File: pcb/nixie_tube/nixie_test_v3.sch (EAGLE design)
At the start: 21 parts, among them IC1 74141N

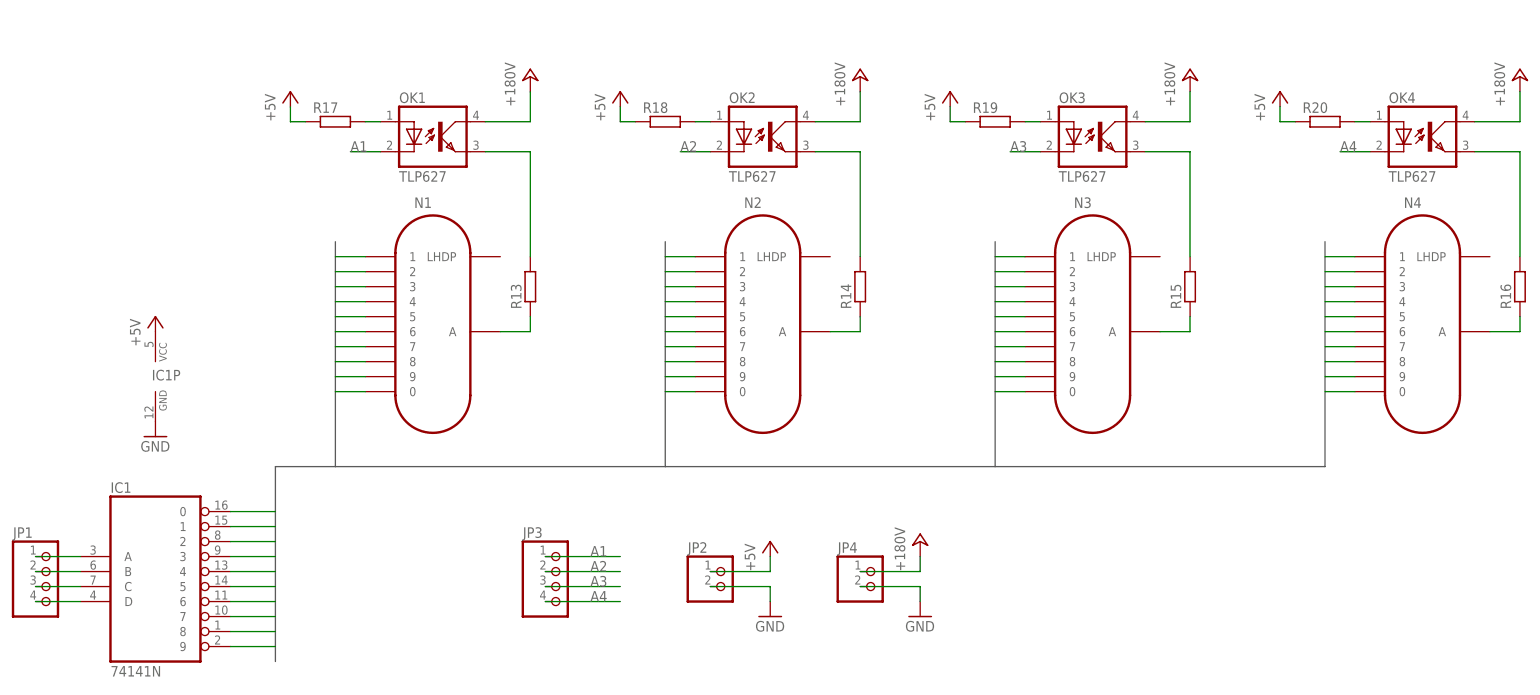
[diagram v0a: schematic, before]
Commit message: 
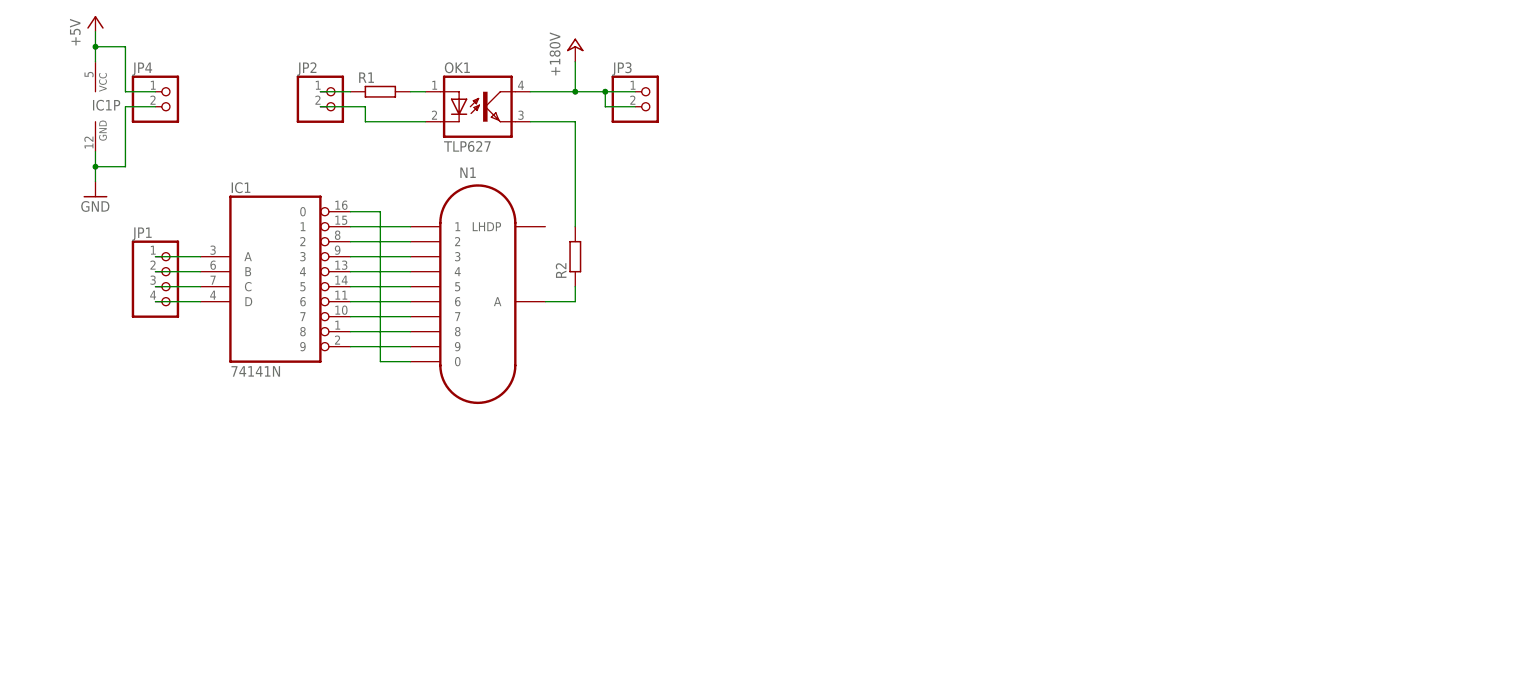
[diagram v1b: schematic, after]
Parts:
- removed N2, N3, N4: IN-12B, nixie_tube:IN-12B
- removed OK2, OK3, OK4: TLP627, nixie_tube:TLP627
- removed R13, R14, R15, R16, R17, R18, R19, R20: (no value), nixie_tube:R-EU_10
- added R1: (no value), nixie_tube:R-EU_R0805
- added R2: (no value), nixie_tube:R-EU_10
- JP3: device nixie_tube:PINHD-1X4 -> nixie_tube:PINHD-1X2
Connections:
- net N$1 renamed A
- net N$2 renamed B
- net N$3 renamed C
- net N$4 renamed D
- removed net A1: JP3.1, OK1.C
- removed net A2: JP3.2, OK2.C
- removed net A3: JP3.3, OK3.C
- removed net A4: JP3.4, OK4.C
- removed net N$13: N1.A, R13.1
- removed net N$14: OK1.EMIT, R13.2
- removed net N$15: N2.A, R14.1
- removed net N$16: OK2.EMIT, R14.2
- removed net N$19: N4.A, R16.1
- removed net N$20: OK4.EMIT, R16.2
- removed net N$21: OK1.A, R17.2
- removed net N$22: OK2.A, R18.2
- removed net N$24: OK4.A, R20.2
- new net N$2: JP2.2, OK1.C
- new net N$6: JP2.1, R1.1
- net +24V: now also JP3.1, JP3.2; no longer JP4.1, OK2.COL, OK3.COL, OK4.COL
- net +5V: now also JP4.1; no longer JP2.1, R17.1, R18.1, R19.1, R20.1
- net C0: no longer N2.0, N3.0, N4.0
- net C1: no longer N2.1, N3.1, N4.1
- net C2: no longer N2.2, N3.2, N4.2
- net C3: no longer N2.3, N3.3, N4.3
- net C4: no longer N2.4, N3.4, N4.4
- net C5: no longer N2.5, N3.5, N4.5
- net C6: no longer N2.6, N3.6, N4.6
- net C7: no longer N2.7, N3.7, N4.7
- net C8: no longer N2.8, N3.8, N4.8
- net C9: no longer N2.9, N3.9, N4.9
- net GND: no longer JP2.2
- net N$17: now also N1.A, R2.1; no longer N3.A, R15.1
- net N$18: now also OK1.EMIT, R2.2; no longer OK3.EMIT, R15.2
- net N$23: now also OK1.A, R1.2; no longer OK3.A, R19.2
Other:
- moved on the sheet: IC1, IC1P, JP1, JP2, JP4, N1, OK1

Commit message: 
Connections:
- net +24V renamed +180V
- net N$2 renamed LK
- net N$6 renamed LA
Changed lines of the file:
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@@
 </segment>
 </net>
-<net name="+24V" class="0">
+<net name="+180V" class="0">
 <segment>
 <pinref part="OK1" gate="G$1" pin="COL"/>
-<pinref part="P+3" gate="1" pin="+24V"/>
+<pinref part="P+3" gate="1" pin="+180V"/>
 <wire x1="55.88" y1="76.2" x2="63.5" y2="76.2" width="0.1524" layer="91"/>
 <wire x1="63.5" y1="76.2" x2="63.5" y2="81.28" width="0.1524" layer="91"/>
@@
 </segment>
 </net>
-<net name="N$2" class="0">
+<net name="LK" class="0">
 <segment>
 <pinref part="JP2" gate="G$1" pin="2"/>
@@
 </segment>
 </net>
-<net name="N$6" class="0">
+<net name="LA" class="0">
 <segment>
 <pinref part="JP2" gate="G$1" pin="1"/>

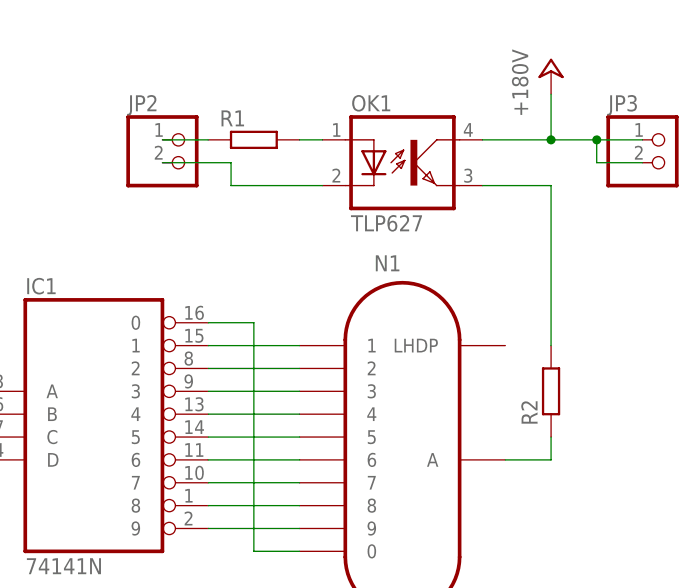
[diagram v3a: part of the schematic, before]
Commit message: 
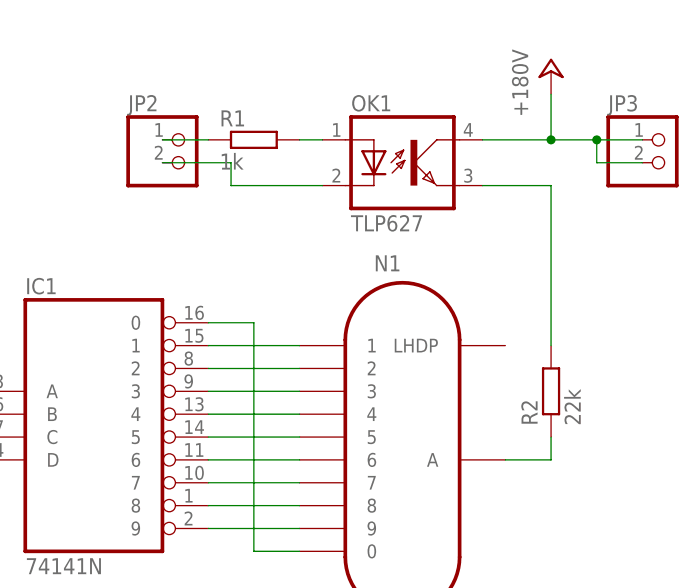
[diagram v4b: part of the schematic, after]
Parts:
- R1: value (none) -> 1k
- R2: value (none) -> 22k
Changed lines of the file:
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@@
 <?xml version="1.0" encoding="utf-8"?>
 <!DOCTYPE eagle SYSTEM "eagle.dtd">
-<eagle version="6.1">
+<eagle version="6.2">
 <drawing>
 <settings>
@@
 <parts>
 <part name="N1" library="nixie_tube" deviceset="IN-12B" device=""/>
-<part name="R2" library="nixie_tube" deviceset="R-EU_" device="10"/>
+<part name="R2" library="nixie_tube" deviceset="R-EU_" device="10" value="22k"/>
 <part name="OK1" library="nixie_tube" deviceset="TLP627" device=""/>
 <part name="P+3" library="nixie_tube" deviceset="+180V" device=""/>
-<part name="R1" library="nixie_tube" deviceset="R-EU_" device="R0805"/>
+<part name="R1" library="nixie_tube" deviceset="R-EU_" device="R0805" value="1k"/>
 <part name="JP2" library="nixie_tube" deviceset="PINHD-1X2" device=""/>
 <part name="JP3" library="nixie_tube" deviceset="PINHD-1X2" device=""/>
